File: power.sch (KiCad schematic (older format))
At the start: 19 parts, among them J1 USB_C_Receptacle_USB2.0, Q1 FS8205, Q2 AO3401A, U2 TP4054, U3 DW01+G, U4 XC6206P332MR

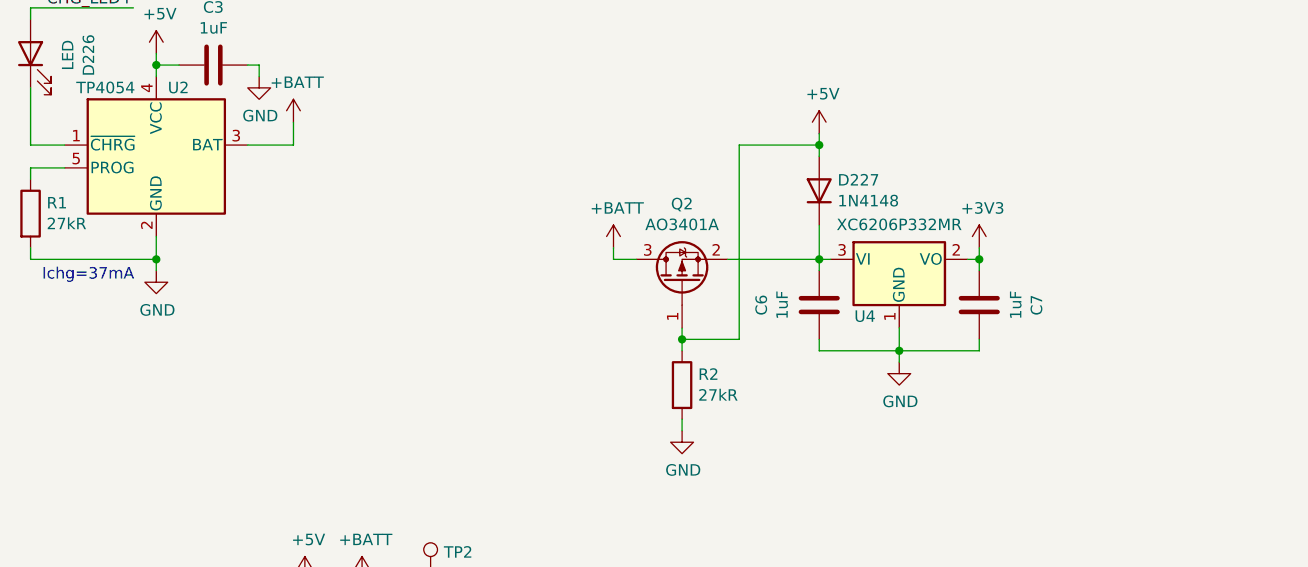
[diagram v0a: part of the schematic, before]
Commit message: Bump up charge current to 45mA
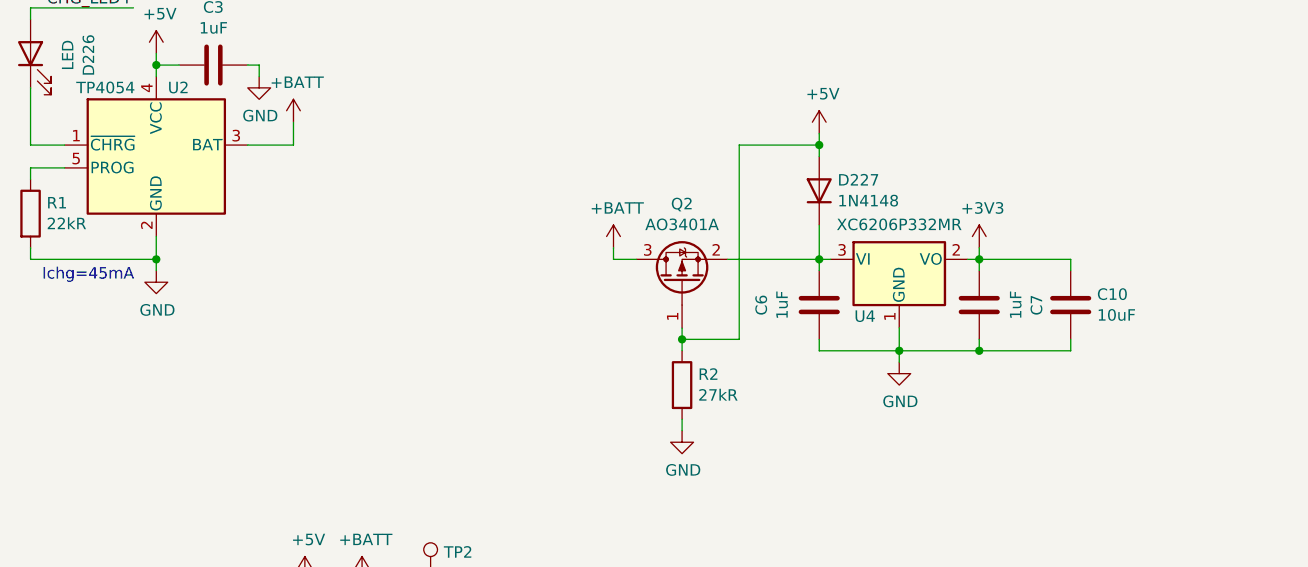
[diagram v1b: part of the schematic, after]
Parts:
- added C10: 10uF, Capacitor_SMD:C_0402_1005Metric, symbol Device:C
- R1: value 27kR -> 22kR; LCSC C25771 -> C25768
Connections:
- net +3V3: now also C10.2
- net GND: now also C10.1
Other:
- note added: "Ichg=45mA"
- note removed: "Ichg=37mA"
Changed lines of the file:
@@
 AR Path="/634EFCCB/63609E91" Ref="R1"  Part="1"
 F 0 "R1" H 1770 2896 50  0000 L CNN
-F 1 "27kR" H 1770 2805 50  0000 L CNN
+F 1 "22kR" H 1770 2805 50  0000 L CNN
 F 2 "Resistor_SMD:R_0402_1005Metric" V 1630 2850 50  0001 C CNN
 F 3 "~" H 1700 2850 50  0001 C CNN
-F 4 "C25771" V 1700 2850 50  0001 C CNN "LCSC"
+F 4 "C25768" V 1700 2850 50  0001 C CNN "LCSC"
 	1    1700 2850
 	1    0    0    -1
 $EndComp
 Text Notes 1750 3150 0    50   ~ 0
-Ichg=37mA
+Ichg=45mA
 Wire Wire Line
 	1850 2650 1700 2650
@@
 Text HLabel 9050 2950 2    50   BiDi ~ 0
 D+
+$Comp
+L Device:C C?
+U 1 1 643AD16D
+P 6250 3250
+AR Path="/643AD16D" Ref="C?"  Part="1"
+AR Path="/634EFCCB/643AD16D" Ref="C10"  Part="1"
+F 0 "C10" H 6135 3204 50  0000 R CNN
+F 1 "10uF" H 6135 3295 50  0000 R CNN
+F 2 "Capacitor_SMD:C_0402_1005Metric" H 6288 3100 50  0001 C CNN
+F 3 "~" H 6250 3250 50  0001 C CNN
+F 4 "C15525" V 6250 3250 50  0001 C CNN "LCSC"
+	1    6250 3250
+	-1   0    0    1
+$EndComp
+Wire Wire Line
+	5850 3050 6250 3050
+Wire Wire Line
+	6250 3050 6250 3100
+Wire Wire Line
+	5850 3450 6250 3450
+Wire Wire Line
+	6250 3450 6250 3400
+Connection ~ 5850 3450
 $EndSCHEMATC

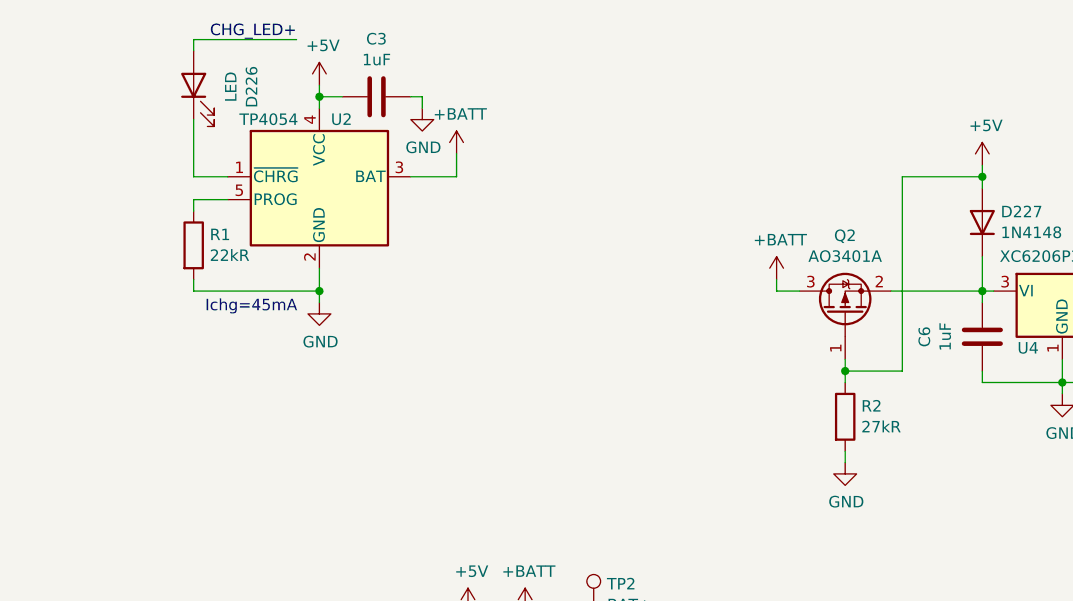
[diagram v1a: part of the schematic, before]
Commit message: Add charge current monitoring
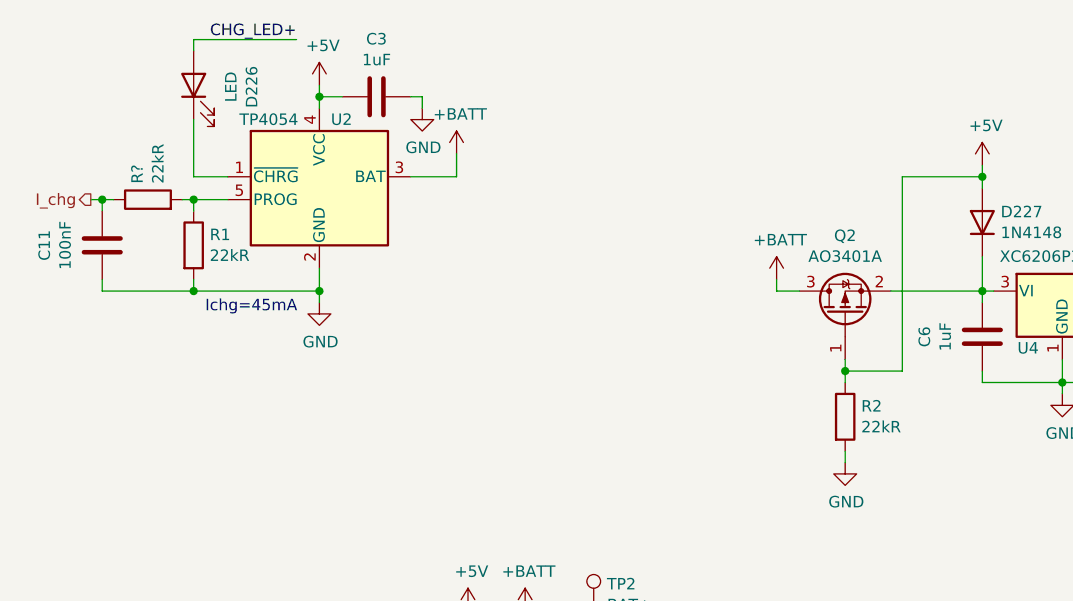
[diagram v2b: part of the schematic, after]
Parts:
- added C11: 100nF, Capacitor_SMD:C_0402_1005Metric, symbol Device:C
- added R?: 22kR, Resistor_SMD:R_0402_1005Metric, symbol Device:R
- R2: value 27kR -> 22kR; LCSC C25771 -> C25768
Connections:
- net GND: now also C11.2
- net at R1.1, U2.5 (PROG): now also R?.2
- new net I_chg: C11.1, R?.1

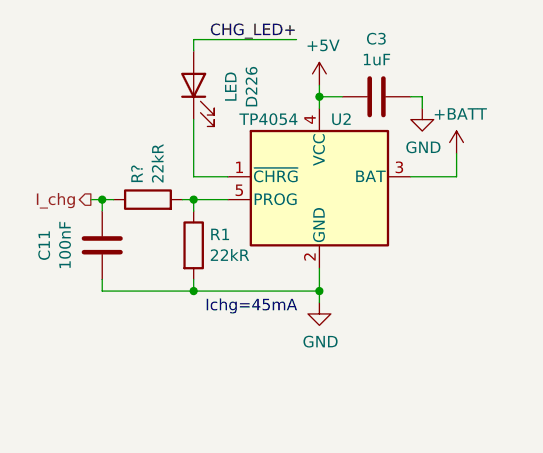
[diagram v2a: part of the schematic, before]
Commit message: Break out BOOT0 to additional GPIO
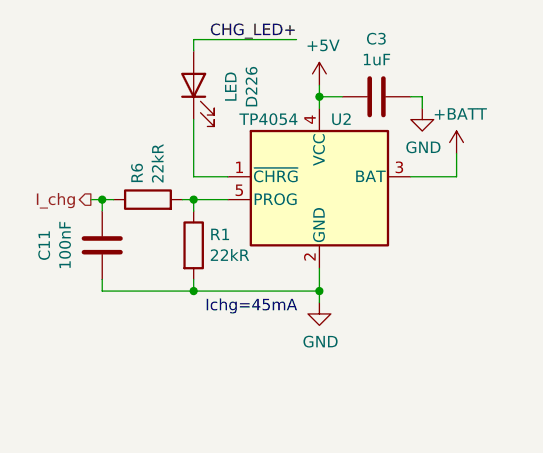
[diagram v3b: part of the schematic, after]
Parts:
- gave numbers to parts that had none: 1
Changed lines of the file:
@@
 P 1500 2650
 AR Path="/644F21C2" Ref="R?"  Part="1"
-AR Path="/634EFCCB/644F21C2" Ref="R?"  Part="1"
-F 0 "R?" H 1570 2696 50  0000 L CNN
+AR Path="/634EFCCB/644F21C2" Ref="R6"  Part="1"
+F 0 "R6" H 1570 2696 50  0000 L CNN
 F 1 "22kR" H 1570 2605 50  0000 L CNN
 F 2 "Resistor_SMD:R_0402_1005Metric" V 1430 2650 50  0001 C CNN
